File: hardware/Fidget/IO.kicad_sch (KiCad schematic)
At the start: 8 parts

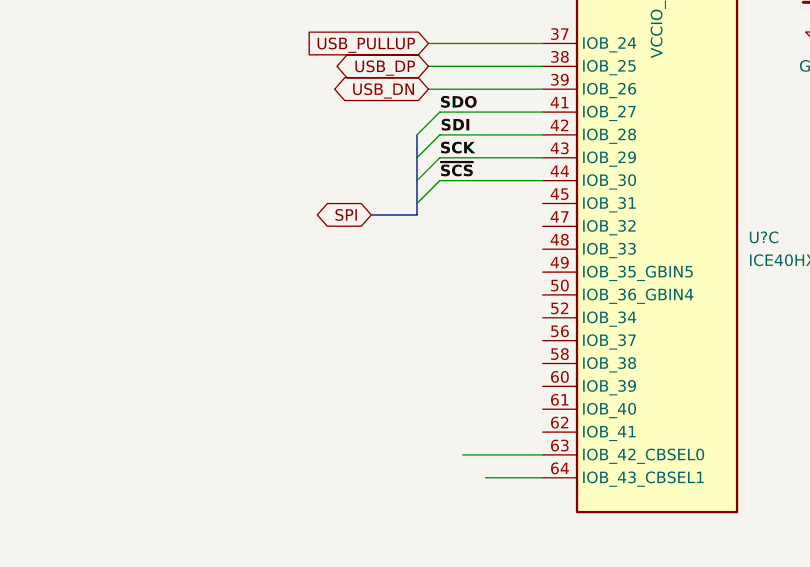
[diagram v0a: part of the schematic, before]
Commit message: Added oscillators
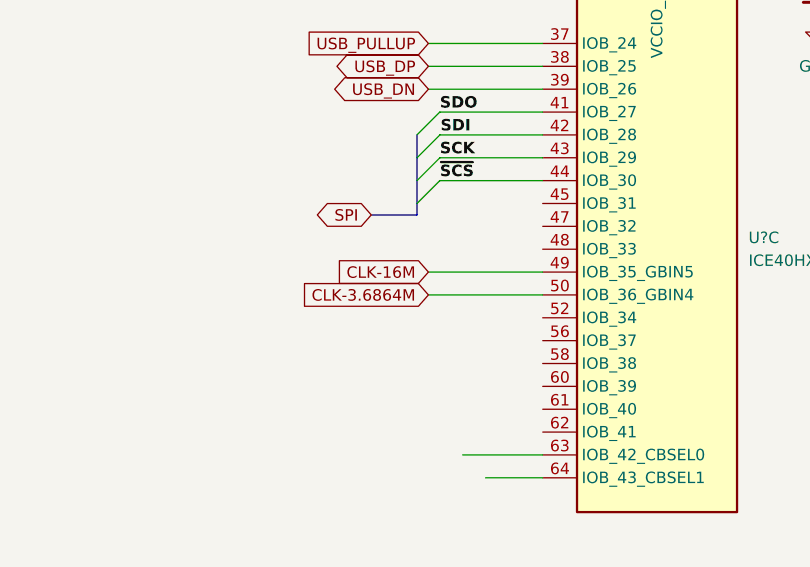
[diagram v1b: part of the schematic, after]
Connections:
- net CLK-16M: now reaches U?.49 (IOB_35_GBIN5)
- net CLK-3.6864M: now reaches U?.50 (IOB_36_GBIN4)
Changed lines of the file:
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@@
+    (stroke (width 0) (type default) (color 0 0 0 0))
+  )
+  (wire (pts (xy 41.91 154.94) (xy 54.61 154.94))
     (stroke (width 0) (type default) (color 0 0 0 0))
   )
@@
   )
   (bus (pts (xy 43.18 34.29) (xy 43.18 36.83))
+    (stroke (width 0) (type default) (color 0 0 0 0))
+  )
+  (wire (pts (xy 41.91 152.4) (xy 54.61 152.4))
     (stroke (width 0) (type default) (color 0 0 0 0))
   )
@@
     )
   )
+  (global_label "CLK-16M" (shape input) (at 41.91 152.4 180) (fields_autoplaced)
+    (effects (font (size 1.27 1.27)) (justify right))
+    (property "Intersheet References" "${INTERSHEET_REFS}" (id 0) (at 30.4859 152.3206 0)
+      (effects (font (size 1.27 1.27)) (justify right) hide)
+    )
+  )
   (global_label "~{BERR_L}" (shape output) (at 115.57 77.47 180) (fields_autoplaced)
     (effects (font (size 1.27 1.27)) (justify right))
@@
       (effects (font (size 1.27 1.27)) (justify right) hide)
     )
+  )
+  (global_label "CLK-3.6864M" (shape input) (at 41.91 154.94 180) (fields_autoplaced)
+    (effects (font (size 1.27 1.27)) (justify right))
+    (property "Intersheet References" "${INTERSHEET_REFS}" (id 0) (at 26.2526 154.8606 0)
+      (effects (font (size 1.27 1.27)) (justify right) hide)
+    )

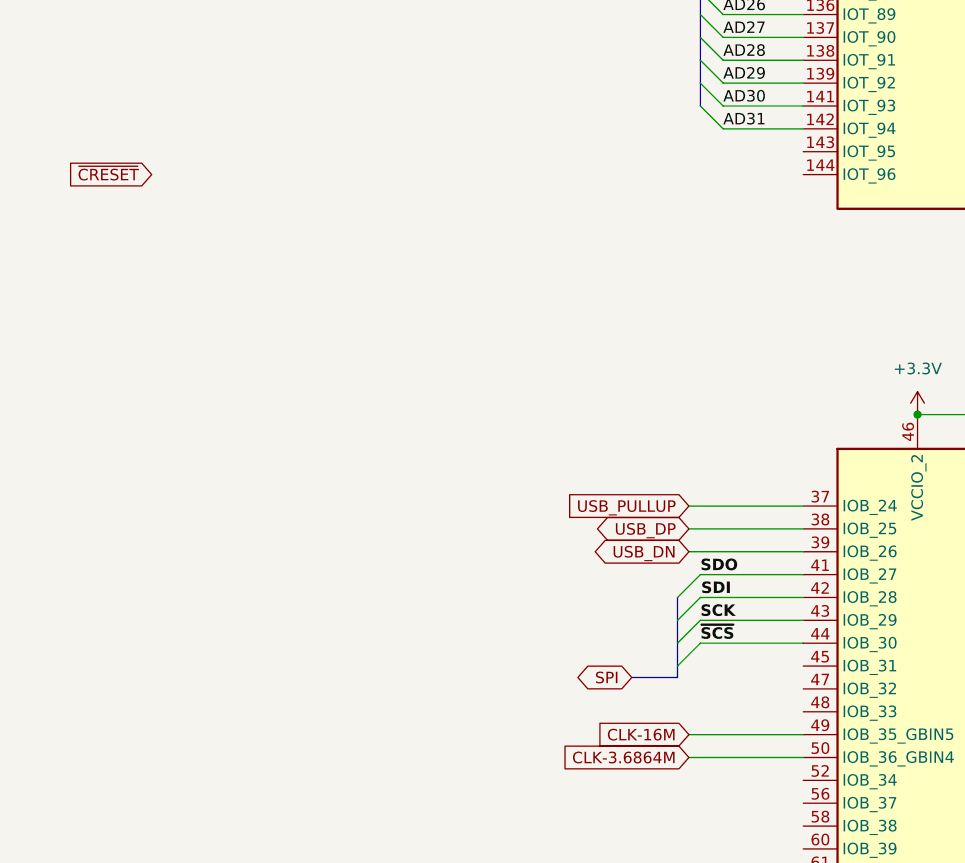
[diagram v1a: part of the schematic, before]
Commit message: Assigned bus control signals to level shifters
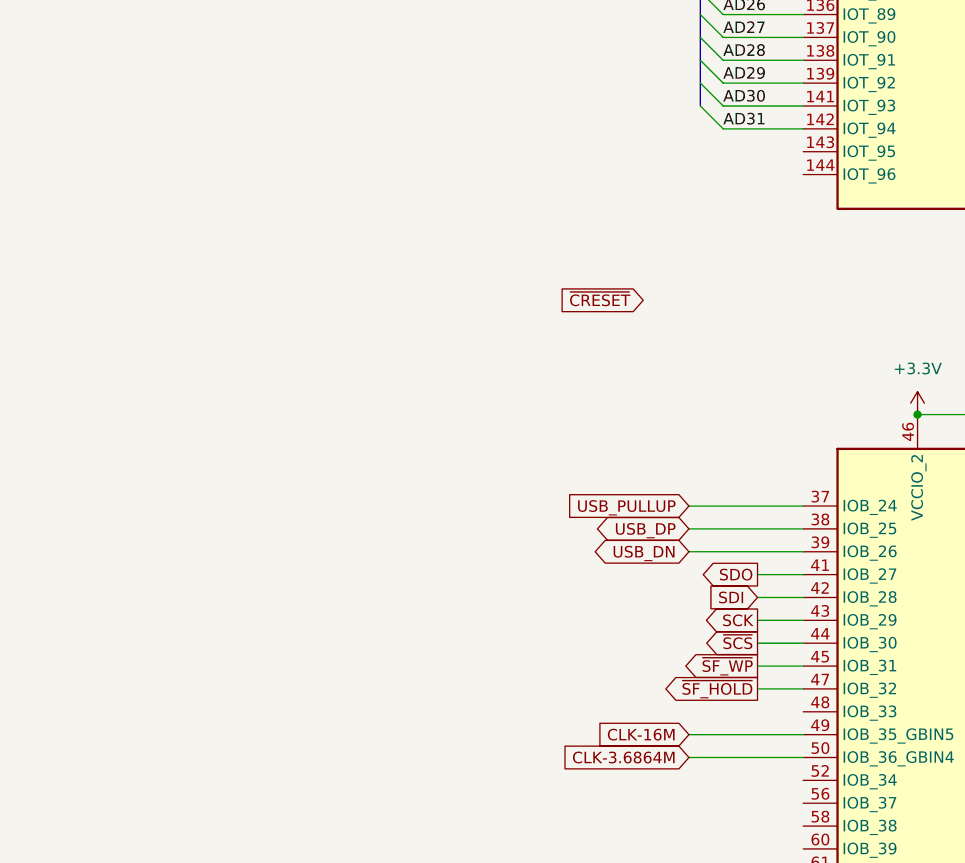
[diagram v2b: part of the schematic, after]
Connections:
- net ~{SF_WP}: now reaches U?.45 (IOB_31)
- net ~{SF_HOLD}: now reaches U?.47 (IOB_32)
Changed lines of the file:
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@@
   (junction (at 67.31 26.67) (diameter 0) (color 0 0 0 0)
   )
-  (bus_entry (at 40.64 142.24) (size 2.54 -2.54)
-    (stroke (width 0) (type default) (color 0 0 0 0))
-  )
   (bus_entry (at 43.18 36.83) (size 2.54 2.54)
     (stroke (width 0) (type default) (color 0 0 0 0))
@@
     (stroke (width 0) (type default) (color 0 0 0 0))
   )
-  (bus_entry (at 40.64 139.7) (size 2.54 -2.54)
-    (stroke (width 0) (type default) (color 0 0 0 0))
-  )
-  (bus_entry (at 40.64 137.16) (size 2.54 -2.54)
-    (stroke (width 0) (type default) (color 0 0 0 0))
-  )
   (bus_entry (at 43.18 67.31) (size 2.54 2.54)
     (stroke (width 0) (type default) (color 0 0 0 0))
@@
     (stroke (width 0) (type default) (color 0 0 0 0))
   )
-  (bus_entry (at 40.64 144.78) (size 2.54 -2.54)
-    (stroke (width 0) (type default) (color 0 0 0 0))
-  )
   (bus_entry (at 132.08 44.45) (size 2.54 2.54)
     (stroke (width 0) (type default) (color 0 0 0 0))
@@
     (stroke (width 0) (type default) (color 0 0 0 0))
   )
-  (bus (pts (xy 40.64 137.16) (xy 40.64 139.7))
-    (stroke (width 0) (type default) (color 0 0 0 0))
-  )
   (wire (pts (xy 45.72 36.83) (xy 54.61 36.83))
     (stroke (width 0) (type default) (color 0 0 0 0))
@@
     (stroke (width 0) (type default) (color 0 0 0 0))
   )
+  (wire (pts (xy 54.61 147.32) (xy 49.53 147.32))
+    (stroke (width 0) (type default) (color 0 0 0 0))
+  )
   (bus (pts (xy 132.08 34.29) (xy 132.08 36.83))
     (stroke (width 0) (type default) (color 0 0 0 0))
@@
     (stroke (width 0) (type default) (color 0 0 0 0))
   )
-  (bus (pts (xy 40.64 144.78) (xy 40.64 146.05))
+  (wire (pts (xy 54.61 139.7) (xy 49.53 139.7))
     (stroke (width 0) (type default) (color 0 0 0 0))
   )
@@
     (stroke (width 0) (type default) (color 0 0 0 0))
   )
-  (wire (pts (xy 43.18 134.62) (xy 54.61 134.62))
-    (stroke (width 0) (type default) (color 0 0 0 0))
-  )
   (wire (pts (xy 114.3 130.81) (xy 120.65 130.81))
     (stroke (width 0) (type default) (color 0 0 0 0))
@@
     (stroke (width 0) (type default) (color 0 0 0 0))
   )
-  (bus (pts (xy 35.56 146.05) (xy 40.64 146.05))
-    (stroke (width 0) (type default) (color 0 0 0 0))
-  )
   (wire (pts (xy 134.62 34.29) (xy 143.51 34.29))
     (stroke (width 0) (type default) (color 0 0 0 0))
@@
     (stroke (width 0) (type default) (color 0 0 0 0))
   )
+  (wire (pts (xy 49.53 137.16) (xy 54.61 137.16))
+    (stroke (width 0) (type default) (color 0 0 0 0))
+  )
   (bus (pts (xy 43.18 36.83) (xy 43.18 39.37))
     (stroke (width 0) (type default) (color 0 0 0 0))
@@
     (stroke (width 0) (type default) (color 0 0 0 0))
   )
-  (wire (pts (xy 43.18 137.16) (xy 54.61 137.16))
-    (stroke (width 0) (type default) (color 0 0 0 0))
-  )
   (wire (pts (xy 115.57 96.52) (xy 121.92 96.52))
     (stroke (width 0) (type default) (color 0 0 0 0))
@@
     (stroke (width 0) (type default) (color 0 0 0 0))
   )
-  (wire (pts (xy 43.18 142.24) (xy 54.61 142.24))
-    (stroke (width 0) (type default) (color 0 0 0 0))
-  )
-  (bus (pts (xy 40.64 139.7) (xy 40.64 142.24))
-    (stroke (width 0) (type default) (color 0 0 0 0))
-  )
   (wire (pts (xy 121.92 77.47) (xy 115.57 77.47))
     (stroke (width 0) (type default) (color 0 0 0 0))
@@
     (stroke (width 0) (type default) (color 0 0 0 0))
   )
+  (wire (pts (xy 54.61 144.78) (xy 49.53 144.78))
+    (stroke (width 0) (type default) (color 0 0 0 0))
+  )
   (wire (pts (xy 114.3 128.27) (xy 120.65 128.27))
     (stroke (width 0) (type default) (color 0 0 0 0))
@@
     (stroke (width 0) (type default) (color 0 0 0 0))
   )
-  (bus (pts (xy 40.64 142.24) (xy 40.64 144.78))
+  (wire (pts (xy 54.61 134.62) (xy 49.53 134.62))
     (stroke (width 0) (type default) (color 0 0 0 0))
   )
@@
     (stroke (width 0) (type default) (color 0 0 0 0))
   )
-  (wire (pts (xy 43.18 139.7) (xy 54.61 139.7))
-    (stroke (width 0) (type default) (color 0 0 0 0))
-  )
   (wire (pts (xy 114.3 60.96) (xy 120.65 60.96))
     (stroke (width 0) (type default) (color 0 0 0 0))
@@
     (stroke (width 0) (type default) (color 0 0 0 0))
   )
+  (wire (pts (xy 54.61 142.24) (xy 49.53 142.24))
+    (stroke (width 0) (type default) (color 0 0 0 0))
+  )
   (wire (pts (xy 45.72 44.45) (xy 54.61 44.45))
     (stroke (width 0) (type default) (color 0 0 0 0))
@@
     (effects (font (size 1.27 1.27)) (justify left bottom))
   )
-  (label "~{SCS}" (at 43.18 142.24 0)
-    (effects (font (size 1.27 1.27) bold) (justify left bottom))
-  )
   (label "AD8" (at 134.62 69.85 0)
     (effects (font (size 1.27 1.27)) (justify left bottom))
@@
     (effects (font (size 1.27 1.27)) (justify left bottom))
   )
-  (label "SDI" (at 43.2577 137.16 0)
-    (effects (font (size 1.27 1.27) bold) (justify left bottom))
-  )
   (label "AD9" (at 134.62 72.39 0)
     (effects (font (size 1.27 1.27)) (justify left bottom))
@@
     (effects (font (size 1.27 1.27)) (justify left bottom))
   )
-  (label "SDO" (at 43.18 134.62 0)
-    (effects (font (size 1.27 1.27) bold) (justify left bottom))
-  )
   (label "AD0" (at 134.62 34.29 0)
     (effects (font (size 1.27 1.27)) (justify left bottom))
@@
     (effects (font (size 1.27 1.27)) (justify left bottom))
   )
-  (label "SCK" (at 43.18 139.7 0)
-    (effects (font (size 1.27 1.27) bold) (justify left bottom))
-  )
   (label "AD23" (at 45.72 52.07 0)
     (effects (font (size 1.27 1.27)) (justify left bottom))
@@
     (effects (font (size 1.27 1.27)) (justify left bottom))
   )
+  (global_label "~{SCS}" (shape output) (at 49.53 142.24 180) (fields_autoplaced)
+    (effects (font (size 1.27 1.27)) (justify right))
+    (property "Intersheet References" "${INTERSHEET_REFS}" (id 0) (at 43.4279 142.1606 0)
+      (effects (font (size 1.27 1.27)) (justify right) hide)
+    )
+  )
   (global_label "USB_PULLUP" (shape input) (at 41.91 127 180) (fields_autoplaced)
     (effects (font (size 1.27 1.27)) (justify right))
@@
     )
   )
+  (global_label "SCK" (shape output) (at 49.53 139.7 180) (fields_autoplaced)
+    (effects (font (size 1.27 1.27)) (justify right))
+    (property "Intersheet References" "${INTERSHEET_REFS}" (id 0) (at 43.3674 139.6206 0)
+      (effects (font (size 1.27 1.27)) (justify right) hide)
+    )
+  )
   (global_label "~{BERR_L}" (shape output) (at 115.57 77.47 180) (fields_autoplaced)
     (effects (font (size 1.27 1.27)) (justify right))
@@
     )
   )
-  (global_label "~{CRESET}" (shape input) (at -17.78 90.17 180) (fields_autoplaced)
-    (effects (font (size 1.27 1.27)) (justify right))
-    (property "Intersheet References" "${INTERSHEET_REFS}" (id 0) (at -27.2083 90.0906 0)
+  (global_label "~{SF_WP}" (shape output) (at 49.53 144.78 180) (fields_autoplaced)
+    (effects (font (size 1.27 1.27)) (justify right))
+    (property "Intersheet References" "${INTERSHEET_REFS}" (id 0) (at 41.1298 144.7006 0)
+      (effects (font (size 1.27 1.27)) (justify right) hide)
+    )
+  )
+  (global_label "~{CRESET}" (shape input) (at 36.83 104.14 180) (fields_autoplaced)
+    (effects (font (size 1.27 1.27)) (justify right))
+    (property "Intersheet References" "${INTERSHEET_REFS}" (id 0) (at 27.4017 104.0606 0)
       (effects (font (size 1.27 1.27)) (justify right) hide)
     )
@@
     )
   )
-  (global_label "SPI" (shape bidirectional) (at 35.56 146.05 180) (fields_autoplaced)
-    (effects (font (size 1.27 1.27)) (justify right))
-    (property "Intersheet References" "${INTERSHEET_REFS}" (id 0) (at 30.0626 146.1294 0)
-      (effects (font (size 1.27 1.27)) (justify right) hide)
-    )
-  )
   (global_label "R{slash}~{W}_L" (shape input) (at 114.3 53.34 180) (fields_autoplaced)
     (effects (font (size 1.27 1.27)) (justify right))
@@
     )
   )
+  (global_label "SDO" (shape output) (at 49.53 134.62 180) (fields_autoplaced)
+    (effects (font (size 1.27 1.27)) (justify right))
+    (property "Intersheet References" "${INTERSHEET_REFS}" (id 0) (at 43.3069 134.5406 0)
+      (effects (font (size 1.27 1.27)) (justify right) hide)
+    )
+  )
+  (global_label "~{SF_HOLD}" (shape output) (at 49.53 147.32 180) (fields_autoplaced)
+    (effects (font (size 1.27 1.27)) (justify right))
+    (property "Intersheet References" "${INTERSHEET_REFS}" (id 0) (at 38.8921 147.2406 0)
+      (effects (font (size 1.27 1.27)) (justify right) hide)
+    )
+  )
   (global_label "SIZ0_L" (shape input) (at 114.3 48.26 180) (fields_autoplaced)
     (effects (font (size 1.27 1.27)) (justify right))
@@
       (effects (font (size 1.27 1.27)) (justify right) hide)
     )
+  )
+  (global_label "SDI" (shape input) (at 49.53 137.16 180) (fields_autoplaced)
+    (effects (font (size 1.27 1.27)) (justify right))
+    (property "Intersheet References" "${INTERSHEET_REFS}" (id 0) (at 44.0326 137.0806 0)
+      (effects (font (size 1.27 1.27)) (justify right) hide)
+    )
